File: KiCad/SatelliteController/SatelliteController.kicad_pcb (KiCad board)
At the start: 2 copper layers, 108 parts, among them J1 CONN_ICSP, J10 FROM_CONVERTER, J11 DC_IN, J2 CONN_USB, J3 USB_B_Micro, J4 RJ45, J5 CONN_PRESS, J6 CONN_STATUS_PANEL, J7 CONN_PANEL_BAORD_1, J8 CONN_PANEL_BAORD_2, J9 TO_CONVERTER, Q1 TJ8S06M3L, Q2 2SC3325-Y, Q3 TJ8S06M3L, SW1 SW_RESET, U1 ATMEGA2560-16AUR, U2 FT232RL, U3 LTC485CN8#PBF, U4 U74HC14, U5 NJM7805SDL1, U6 INA219BIDCNT, U7 INA219BIDCNT, Y1 HUSG-16.000-20

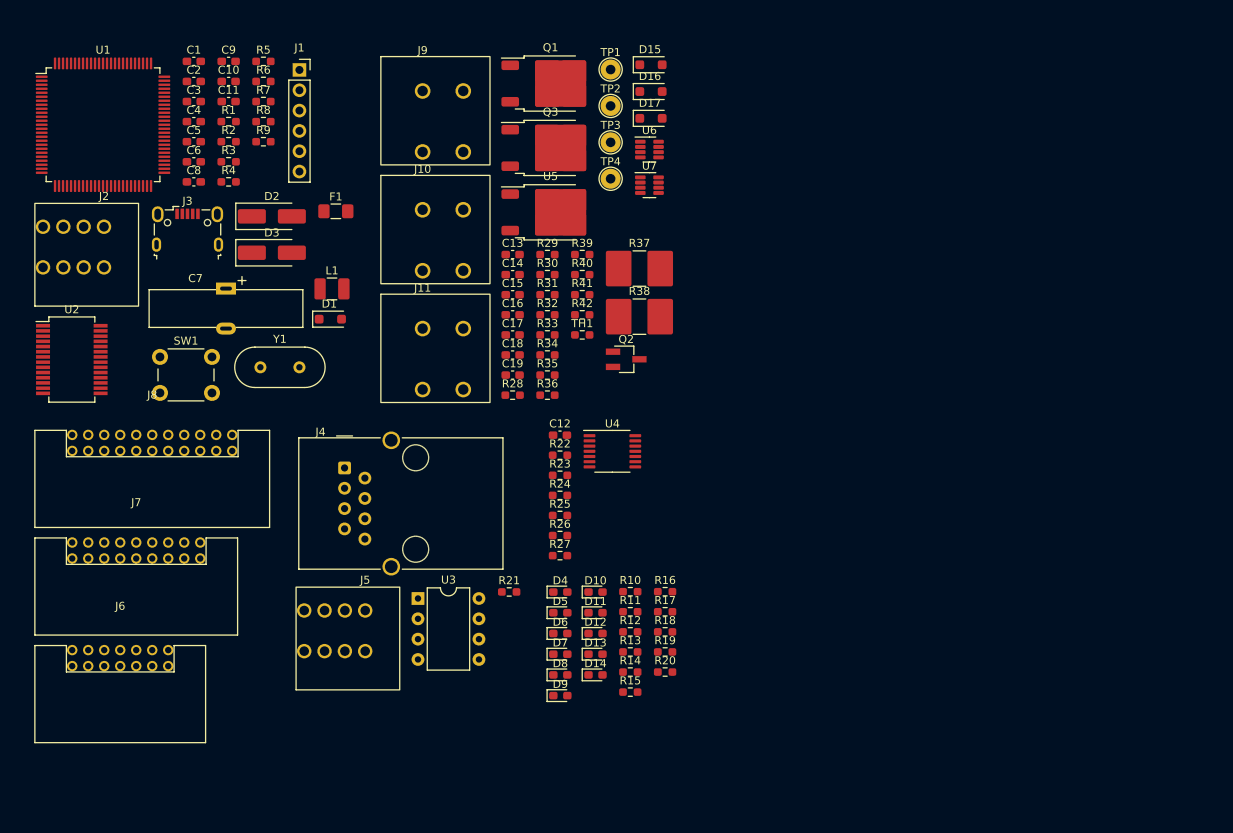
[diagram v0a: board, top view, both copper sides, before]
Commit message: ランコンのKiCadプロジェクトをコピーしてサテコンを作成
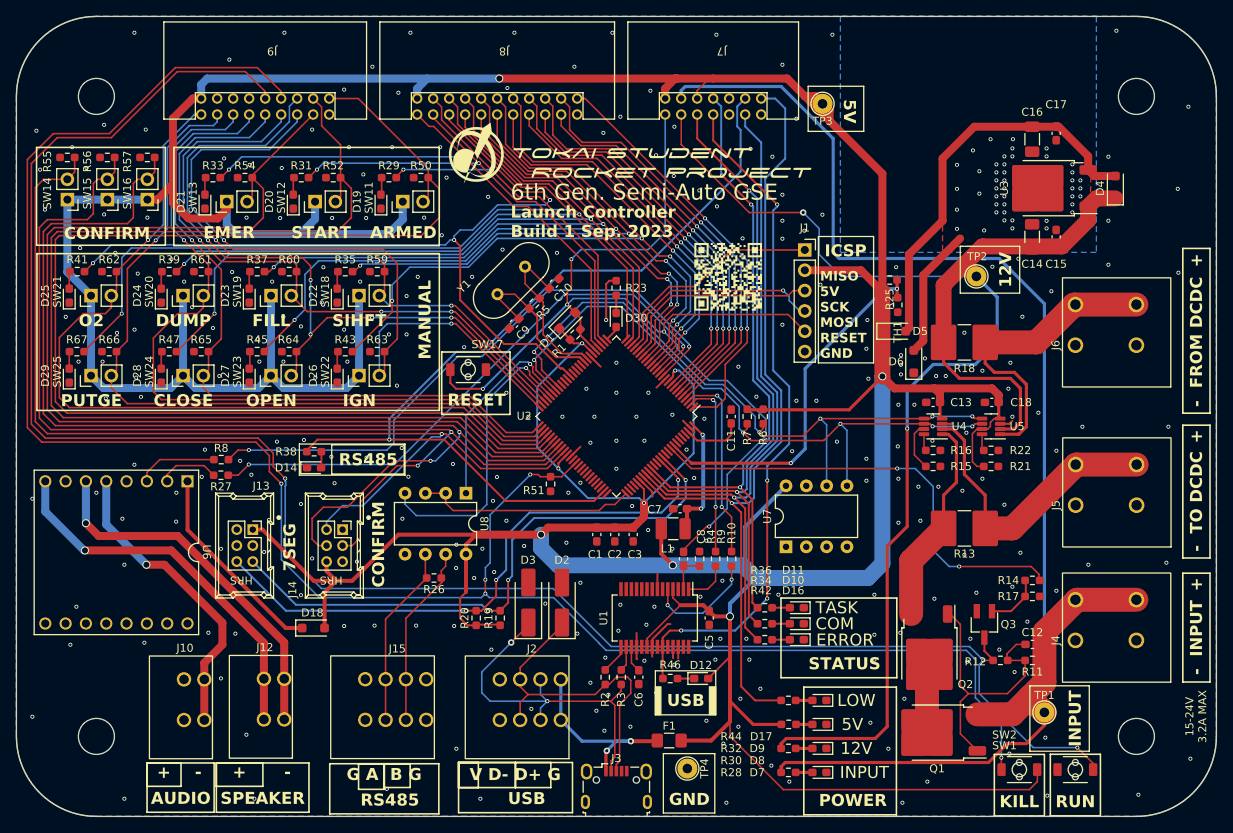
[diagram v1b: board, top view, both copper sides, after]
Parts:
- removed C19, C4: 0.1uF, Capacitor_SMD:C_0603_1608Metric_Pad1.08x0.95mm_HandSolder
- removed D13: LED, LED_SMD:LED_0603_1608Metric_Pad1.05x0.95mm_HandSolder
- removed D15: GS1010FL, Diode_SMD:D_SOD-123F
- removed J11: DC_IN, TSRP_TerminalBlock_Alphaplus:TB411-2-2-E-1
- removed R24: 1kR, Resistor_SMD:R_0603_1608Metric_Pad0.98x0.95mm_HandSolder
- removed R40: 10kR, Resistor_SMD:R_0603_1608Metric_Pad0.98x0.95mm_HandSolder
- added D18: GS1010FL, Diode_SMD:D_SOD-123F, F.Cu at (84.8, 107.3)
- added D19: LED_O, LED_SMD:LED_0603_1608Metric_Pad1.05x0.95mm_HandSolder, F.Cu at (93.2, 54.0)
- added D20: LED_O, LED_SMD:LED_0603_1608Metric_Pad1.05x0.95mm_HandSolder, F.Cu at (82.2, 54.0)
- added D21: LED_O, LED_SMD:LED_0603_1608Metric_Pad1.05x0.95mm_HandSolder, F.Cu at (71.2, 54.0)
- added D22: LED_O, LED_SMD:LED_0603_1608Metric_Pad1.05x0.95mm_HandSolder, F.Cu at (87.7, 65.8)
- added D23: LED_O, LED_SMD:LED_0603_1608Metric_Pad1.05x0.95mm_HandSolder, F.Cu at (76.7, 65.8)
- added D24: LED_O, LED_SMD:LED_0603_1608Metric_Pad1.05x0.95mm_HandSolder, F.Cu at (65.7, 65.8)
- added D25: LED_O, LED_SMD:LED_0603_1608Metric_Pad1.05x0.95mm_HandSolder, F.Cu at (54.2, 65.8)
- added D26: LED_O, LED_SMD:LED_0603_1608Metric_Pad1.05x0.95mm_HandSolder, F.Cu at (87.7, 75.8)
- added D27: LED_O, LED_SMD:LED_0603_1608Metric_Pad1.05x0.95mm_HandSolder, F.Cu at (76.7, 75.8)
- added D28: LED_O, LED_SMD:LED_0603_1608Metric_Pad1.05x0.95mm_HandSolder, F.Cu at (65.7, 75.8)
- added D29: LED_O, LED_SMD:LED_0603_1608Metric_Pad1.05x0.95mm_HandSolder, F.Cu at (54.2, 75.8)
- added D30: LED_O, LED_SMD:LED_0603_1608Metric_Pad1.05x0.95mm_HandSolder, F.Cu at (122.6, 68.8)
- added G***: LOGO, LOGO, F.Cu at (136.6, 63.4)
- added G***: LOGO, LOGO, F.Cu at (124.4, 48.0)
- added J12: CONN_SPEAKER, TSRP_TerminalBlock_Alphaplus:TB401-1-2-E, F.Cu at (78.6, 113.6)
- added J13: CONN_7SEG, TSRP_Connector_Hirose:DF51A-6DP-2DSA, F.Cu at (76.2, 97.0)
- added J14: CONN_BOARD_3, TSRP_Connector_Hirose:DF51A-6DP-2DSA, F.Cu at (87.4, 97.0)
- added J15: CONN_RS485, TSRP_TerminalBlock_Alphaplus:TB401-1-4-E, F.Cu at (95.2, 113.7)
- added R43: 1kR, Resistor_SMD:R_0603_1608Metric_Pad0.98x0.95mm_HandSolder, F.Cu at (88.7, 72.8)
- added R44: 1kR, Resistor_SMD:R_0603_1608Metric_Pad0.98x0.95mm_HandSolder, F.Cu at (144.1, 116.3)
- added R45: 1kR, Resistor_SMD:R_0603_1608Metric_Pad0.98x0.95mm_HandSolder, F.Cu at (77.7, 72.8)
- added R46: 1kR, Resistor_SMD:R_0603_1608Metric_Pad0.98x0.95mm_HandSolder, F.Cu at (129.4, 113.6)
- added R47: 1kR, Resistor_SMD:R_0603_1608Metric_Pad0.98x0.95mm_HandSolder, F.Cu at (66.7, 72.8)
- added R50: 1kR, Resistor_SMD:R_0603_1608Metric_Pad0.98x0.95mm_HandSolder, F.Cu at (98.2, 51.0)
- added R51: 1kR, Resistor_SMD:R_0603_1608Metric_Pad0.98x0.95mm_HandSolder, F.Cu at (114.4, 89.3)
- added R52: 1kR, Resistor_SMD:R_0603_1608Metric_Pad0.98x0.95mm_HandSolder, F.Cu at (87.2, 51.0)
- added R54: 1kR, Resistor_SMD:R_0603_1608Metric_Pad0.98x0.95mm_HandSolder, F.Cu at (76.2, 51.0)
- added R55: 1kR, Resistor_SMD:R_0603_1608Metric_Pad0.98x0.95mm_HandSolder, F.Cu at (54.0, 48.5)
- added R56: 1kR, Resistor_SMD:R_0603_1608Metric_Pad0.98x0.95mm_HandSolder, F.Cu at (59.0, 48.5)
- added R57: 1kR, Resistor_SMD:R_0603_1608Metric_Pad0.98x0.95mm_HandSolder, F.Cu at (64.0, 48.5)
- added R59: 1kR, Resistor_SMD:R_0603_1608Metric_Pad0.98x0.95mm_HandSolder, F.Cu at (92.7, 62.8)
- added R60: 1kR, Resistor_SMD:R_0603_1608Metric_Pad0.98x0.95mm_HandSolder, F.Cu at (81.7, 62.8)
- added R61: 1kR, Resistor_SMD:R_0603_1608Metric_Pad0.98x0.95mm_HandSolder, F.Cu at (70.7, 62.8)
- added R62: 1kR, Resistor_SMD:R_0603_1608Metric_Pad0.98x0.95mm_HandSolder, F.Cu at (59.2, 62.8)
- added R63: 1kR, Resistor_SMD:R_0603_1608Metric_Pad0.98x0.95mm_HandSolder, F.Cu at (92.7, 72.8)
- added R64: 1kR, Resistor_SMD:R_0603_1608Metric_Pad0.98x0.95mm_HandSolder, F.Cu at (81.7, 72.8)
- added R65: 1kR, Resistor_SMD:R_0603_1608Metric_Pad0.98x0.95mm_HandSolder, F.Cu at (70.7, 72.8)
- added R66: 1kR, Resistor_SMD:R_0603_1608Metric_Pad0.98x0.95mm_HandSolder, F.Cu at (59.2, 72.8)
- added R67: 1kR, Resistor_SMD:R_0603_1608Metric_Pad0.98x0.95mm_HandSolder, F.Cu at (55.2, 72.8)
- added REF**: MountingHole_4.5mm, MountingHole:MountingHole_4.5mm, F.Cu at (187.6, 120.8)
- added REF**: MountingHole_4.5mm, MountingHole:MountingHole_4.5mm, F.Cu at (57.6, 40.8)
- added REF**: MountingHole_4.5mm, MountingHole:MountingHole_4.5mm, F.Cu at (57.6, 120.8)
- added REF**: MountingHole_4.5mm, MountingHole:MountingHole_4.5mm, F.Cu at (187.6, 40.8)
- added SW11: SW_Push, Connector_PinHeader_2.54mm:PinHeader_1x02_P2.54mm_Vertical, F.Cu at (95.9, 54.0)
- added SW12: SW_Push, Connector_PinHeader_2.54mm:PinHeader_1x02_P2.54mm_Vertical, F.Cu at (85.0, 54.0)
- added SW13: SW_Push, Connector_PinHeader_2.54mm:PinHeader_1x02_P2.54mm_Vertical, F.Cu at (73.9, 54.0)
- added SW14: SW_Push, Connector_PinHeader_2.54mm:PinHeader_1x02_P2.54mm_Vertical, F.Cu at (54.0, 53.8)
- added SW15: SW_Push, Connector_PinHeader_2.54mm:PinHeader_1x02_P2.54mm_Vertical, F.Cu at (59.0, 53.8)
- added SW16: SW_Push, Connector_PinHeader_2.54mm:PinHeader_1x02_P2.54mm_Vertical, F.Cu at (64.0, 53.8)
- added SW17: SW_Push, TSRP_Button_Switch_SMD:TVAF06-A020B-R, F.Cu at (104.1, 75.0)
- added SW18: SW_Push, Connector_PinHeader_2.54mm:PinHeader_1x02_P2.54mm_Vertical, F.Cu at (90.5, 65.8)
- added SW19: SW_Push, Connector_PinHeader_2.54mm:PinHeader_1x02_P2.54mm_Vertical, F.Cu at (79.5, 65.8)
- added SW2: SW_Push, TSRP_Button_Switch_SMD:TVAF06-A020B-R, F.Cu at (173.0, 125.0)
- added SW20: SW_Push, Connector_PinHeader_2.54mm:PinHeader_1x02_P2.54mm_Vertical, F.Cu at (68.5, 65.8)
- added SW21: SW_Push, Connector_PinHeader_2.54mm:PinHeader_1x02_P2.54mm_Vertical, F.Cu at (57.0, 65.8)
- added SW22: SW_Push, Connector_PinHeader_2.54mm:PinHeader_1x02_P2.54mm_Vertical, F.Cu at (90.5, 75.8)
- added SW23: SW_Push, Connector_PinHeader_2.54mm:PinHeader_1x02_P2.54mm_Vertical, F.Cu at (79.5, 75.8)
- added SW24: SW_Push, Connector_PinHeader_2.54mm:PinHeader_1x02_P2.54mm_Vertical, F.Cu at (68.5, 75.8)
- added SW25: SW_Push, Connector_PinHeader_2.54mm:PinHeader_1x02_P2.54mm_Vertical, F.Cu at (57.0, 75.8)
- added U8: LTC485CN8#PBF, Package_DIP:DIP-8_W7.62mm, F.Cu at (103.8, 90.4)
- C1, C2: value 15pF -> 0.1uF
- C10, C9: value 0.1uF -> 15pF
- C14, C16: footprint Capacitor_SMD:C_0603_1608Metric_Pad1.08x0.95mm_HandSolder -> Capacitor_SMD:C_1206_3216Metric_Pad1.33x1.80mm_HandSolder
- C7: value 1F -> 0.1uF; footprint Capacitor_THT:DX_5R5VxxxxU_D19.0mm_P5.00mm -> Capacitor_SMD:C_0603_1608Metric_Pad1.08x0.95mm_HandSolder
- D10, D11: value LED -> LED_G
- D12, D14: value LED -> LED_B
- D16, D17: value SS2040FL -> LED_R; footprint Diode_SMD:D_SOD-123F -> LED_SMD:LED_0603_1608Metric_Pad1.05x0.95mm_HandSolder
- D4: value LED -> GS1010FL; footprint LED_SMD:LED_0603_1608Metric_Pad1.05x0.95mm_HandSolder -> Diode_SMD:D_SOD-123F
- D5, D6: value LED -> SS2040FL; footprint LED_SMD:LED_0603_1608Metric_Pad1.05x0.95mm_HandSolder -> Diode_SMD:D_SOD-123F
- D7, D8, D9: value LED -> LED_O
- J10: value FROM_CONVERTER -> CONN_AUDIO; footprint TSRP_TerminalBlock_Alphaplus:TB411-2-2-E-1 -> TSRP_TerminalBlock_Alphaplus:TB401-1-2-E
- J4: value RJ45 -> DC_IN; footprint Connector_RJ:RJ45_Wuerth_7499010001A_Horizontal -> TSRP_TerminalBlock_Alphaplus:TB411-2-2-E-1
- J5: value CONN_PRESS -> TO_CONVERTER; footprint TSRP_TerminalBlock_Alphaplus:TB401-1-4-E -> TSRP_TerminalBlock_Alphaplus:TB411-2-2-E-1
- J6: value CONN_STATUS_PANEL -> FROM_CONVERTER; footprint TSRP_Connector_Hirose:DF51A-14DP-2DS -> TSRP_TerminalBlock_Alphaplus:TB411-2-2-E-1
- J7: value CONN_PANEL_BAORD_1 -> CONN_STATUS_PANEL; footprint TSRP_Connector_Hirose:DF51A-18DP-2DS -> TSRP_Connector_Hirose:DF51A-14DP-2DS
- J9: value TO_CONVERTER -> CONN_PANEL_BAORD_1; footprint TSRP_TerminalBlock_Alphaplus:TB411-2-2-E-1 -> TSRP_Connector_Hirose:DF51A-18DP-2DS
- Q2: value 2SC3325-Y -> TJ8S06M3L; footprint Package_TO_SOT_SMD:SC-59_Handsoldering -> Package_TO_SOT_SMD:TO-252-2
- Q3: value TJ8S06M3L -> 2SC3325-Y; footprint Package_TO_SOT_SMD:TO-252-2 -> Package_TO_SOT_SMD:SC-59_Handsoldering
- R10: value 3.6kR -> 1kR
- R11: value 1kR -> 5.6R
- R12: value 2.4kR -> 3.3R
- R13, R18: value 1kR -> 0.1R2W; footprint Resistor_SMD:R_0603_1608Metric_Pad0.98x0.95mm_HandSolder -> Resistor_SMD:R_2816_7142Metric_Pad3.20x4.45mm_HandSolder
- R14, R15, R16, R17, R19, R20, R22, R25: value 1kR -> 10kR
- R2: value 1MR -> 22R
- R21: value 120R -> 10kR
- R26: value 1kR -> 120R
- R28: value 5.6R -> 3.6kR
- R29: value 3.3R -> 1kR
- R3: value 1kR -> 22R
- R30: value 10kR -> 2.4kR
- R31: value 2.2kR -> 1kR
- R32: value 12kR -> 1kR
- R33, R35: value 2kR -> 1kR
- R34: value 12kR -> 2.2kR
- R36: value 10kR -> 2.2kR
- R37, R38: value 0.1R2W -> 1kR; footprint Resistor_SMD:R_2816_7142Metric_Pad3.20x4.45mm_HandSolder -> Resistor_SMD:R_0603_1608Metric_Pad0.98x0.95mm_HandSolder
- R39, R41, R42: value 10kR -> 1kR
- R5: value 10kR -> 1MR
- R7: value 22R -> 10kR
- R8: value 22R -> 1kR
- SW1: value SW_RESET -> SW_Push; footprint Button_Switch_THT:SW_PUSH_6mm_H7.3mm -> TSRP_Button_Switch_SMD:TVAF06-A020B-R
- U1: value ATMEGA2560-16AUR -> FT232RL; footprint Package_QFP:TQFP-100_14x14mm_P0.5mm -> Package_SO:SSOP-28_5.3x10.2mm_P0.65mm
- U2: value FT232RL -> ATMEGA2560-16AUR; footprint Package_SO:SSOP-28_5.3x10.2mm_P0.65mm -> Package_QFP:TQFP-100_14x14mm_P0.5mm
- U3: value LTC485CN8#PBF -> NJM7805SDL1; footprint Package_DIP:DIP-8_W7.62mm -> Package_TO_SOT_SMD:TO-252-2
- U4: value U74HC14 -> INA219BIDCNT; footprint Package_SO:TSSOP-14_4.4x5mm_P0.65mm -> Package_TO_SOT_SMD:SOT-23-8
- U5: value NJM7805SDL1 -> INA219BIDCNT; footprint Package_TO_SOT_SMD:TO-252-2 -> Package_TO_SOT_SMD:SOT-23-8
- U6: value INA219BIDCNT -> DFPlayer; footprint Package_TO_SOT_SMD:SOT-23-8 -> TSRP_Module:DFPlayer-mini
- U7: value INA219BIDCNT -> 24LC256; footprint Package_TO_SOT_SMD:SOT-23-8 -> Package_DIP:DIP-8_W7.62mm
- moved J6 133.6 mm to (182.6, 71.9), turned to 90 degrees
- moved SW1 125.5 mm to (180.0, 125.0)
- moved J7 101.4 mm to (140.7, 43.1), turned to 180 degrees
- moved TP1 96.9 mm to (176.1, 117.8)
- moved J4 96.4 mm to (182.6, 108.8), turned to 90 degrees
- moved Q1 94.4 mm to (162.7, 120.4), turned to 180 degrees
- moved U3 94.0 mm to (176.6, 52.3), turned to 180 degrees
- moved U1 92.5 mm to (127.4, 106.0), turned to -90 degrees
- moved J5 92.4 mm to (182.7, 91.9), turned to 90 degrees
- moved J3 87.9 mm to (122.6, 127.1)
- moved C5 87.7 mm to (134.2, 106.0), turned to 90 degrees
- moved D4 85.9 mm to (185.0, 52.2), turned to 90 degrees
- moved C6 85.1 mm to (125.4, 113.4), turned to 90 degrees
- moved R2 81.8 mm to (121.2, 113.4), turned to 90 degrees
- moved R3 81.0 mm to (123.2, 113.4), turned to -90 degrees
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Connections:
- C1 pad 1: GND -> CONN_LED_5V
- C1 pad 2: Net-(U1-XTAL1) -> GND
- C10 pad 2: +5V -> Net-(U2-XTAL2)
- C11 pad 1: Net-(U2-DTR) -> GND
- C11 pad 2: CTL_RESET -> Net-(U2-AREF)
- C12 pad 1: GND -> CONN_LED_INPUT
- C12 pad 2: +5V -> Net-(Q1-G)
- C13 pad 1: CONN_LED_INPUT -> CONN_LED_5V
- C13 pad 2: Net-(Q1-G) -> GND
- C14 pad 1: Net-(D16-A) -> Net-(D6-A)
- C15 pad 1: Net-(D16-A) -> Net-(D6-A)
- C16 pad 1: Net-(D16-A) -> Net-(D6-A)
- C16 pad 2: Net-(D15-A) -> Net-(D4-A)
- C17 pad 1: Net-(D16-A) -> Net-(D6-A)
- C17 pad 2: Net-(D15-A) -> Net-(D4-A)
- C2 pad 1: GND -> CONN_LED_5V
- C2 pad 2: Net-(U1-XTAL2) -> GND
- C3 pad 1: GND -> CONN_LED_5V
- C3 pad 2: Net-(U1-AREF) -> GND
- C5 pad 1: +5V -> GND
- C5 pad 2: GND -> CONN_LED_5V
- C6 pad 1: +5V -> GND
- C6 pad 2: GND -> Net-(U1-3V3OUT)
- C7 pad 1: +5V -> Net-(U2-AVCC)
- C8 pad 1: Net-(U1-AVCC) -> Net-(U1-DTR)
- C8 pad 2: GND -> CTL_RESET
- C9 pad 2: Net-(U2-3V3OUT) -> Net-(U2-XTAL1)
- D1 pad 1: +5V -> CONN_LED_5V
- D12 pad 1: GND -> Net-(D12-K)
- D12 pad 2: Net-(D12-A) -> CONN_LED_5V
- D17 pad 1: CONN_LED_5V -> GND
- D17 pad 2: Net-(D15-A) -> Net-(D17-A)
- D2 pad 1: GND -> USB_D+
- D2 pad 2: USB_D+ -> GND
- D3 pad 1: GND -> USB_D-
- D3 pad 2: USB_D- -> GND
- D4 pad 1: GND -> CONN_LED_12V
- D5 pad 1: Net-(D5-K) -> CONN_LED_5V
- D5 pad 2: +5V -> Net-(D4-A)
- D7 pad 1: Net-(D7-K) -> GND
- D7 pad 2: +5V -> Net-(D7-A)
- F1 pad 2: +5V -> CONN_LED_5V
- J1 pad 2: +5V -> CONN_LED_5V
- J10 pad 2: FROM_CONVERTER -> Net-(J10-Pin_2)
- J4 pad 2: GND -> CONN_LED_INPUT
- J5 pad 1: +12V -> GND
- J5 pad 2: unconnected-(J5-Pin_2-Pad2) -> TO_CONVERTER
- J6 pad 2: CONN_LED_LOW_VOLTAGE -> FROM_CONVERTER
- J7 pad 10: unconnected-(J7-Pin_10-Pad10) -> CONN_LED_5V
- J7 pad 11: unconnected-(J7-Pin_11-Pad11) -> CONN_LED_12V
- J7 pad 12: unconnected-(J7-Pin_12-Pad12) -> CONN_LED_INPUT
- J7 pad 13: unconnected-(J7-Pin_13-Pad13) -> CTL_RESET
- J7 pad 14: unconnected-(J7-Pin_14-Pad14) -> CONN_LED_5V
- J7 pad 2: unconnected-(J7-Pin_2-Pad2) -> CONN_LED_LOW_VOLTAGE
- J7 pad 3: unconnected-(J7-Pin_3-Pad3) -> CONN_LED_ERROR
- J7 pad 4: unconnected-(J7-Pin_4-Pad4) -> CONN_LED_RS485_ACCESS
- J7 pad 7: unconnected-(J7-Pin_7-Pad7) -> CONN_LED_USB_ACCESS
- J7 pad 8: unconnected-(J7-Pin_8-Pad8) -> CONN_LED_TASK
- J7 pad 9: unconnected-(J7-Pin_9-Pad9) -> CONN_LED_COM
- J8 pad 10: unconnected-(J8-Pin_10-Pad10) -> CONN_LED_FB_PURGE
- J8 pad 11: unconnected-(J8-Pin_11-Pad11) -> CONN_LED_SHIFT
- J8 pad 12: unconnected-(J8-Pin_12-Pad12) -> CONN_LED_IGNITOR
- J8 pad 13: unconnected-(J8-Pin_13-Pad13) -> CONN_LED_FILL
- J8 pad 14: unconnected-(J8-Pin_14-Pad14) -> CONN_LED_OPEN
- J8 pad 15: unconnected-(J8-Pin_15-Pad15) -> CONN_LED_DUMP
- J8 pad 16: unconnected-(J8-Pin_16-Pad16) -> CONN_LED_CLOSE
- J8 pad 17: unconnected-(J8-Pin_17-Pad17) -> CONN_LED_O2
- J8 pad 18: unconnected-(J8-Pin_18-Pad18) -> CONN_LED_PURGE
- J8 pad 19: unconnected-(J8-Pin_19-Pad19) -> CONN_LED_SEQUENCE
- J8 pad 2: unconnected-(J8-Pin_2-Pad2) -> CONN_LED_POWER
- J8 pad 20: unconnected-(J8-Pin_20-Pad20) -> CONN_LED_SAFTEY
- J8 pad 21: unconnected-(J8-Pin_21-Pad21) -> CONN_LED_EMERGENCY
- J8 pad 22: +5V -> CONN_LED_5V
- J8 pad 3: unconnected-(J8-Pin_3-Pad3) -> CONN_LED_FB_SHIFT
- J8 pad 4: unconnected-(J8-Pin_4-Pad4) -> CONN_LED_FB_IGNITOR
- J8 pad 5: unconnected-(J8-Pin_5-Pad5) -> CONN_LED_FB_FILL
- J8 pad 6: unconnected-(J8-Pin_6-Pad6) -> CONN_LED_FB_OPEN
- J8 pad 7: unconnected-(J8-Pin_7-Pad7) -> CONN_LED_FB_DUMP
- J8 pad 8: unconnected-(J8-Pin_8-Pad8) -> CONN_LED_FB_CLOSE
- J8 pad 9: unconnected-(J8-Pin_9-Pad9) -> CONN_LED_FB_O2
- J9 pad 2: TO_CONVERTER -> CTL_SAFETY
- L1 pad 1: Net-(U1-AVCC) -> Net-(U2-AVCC)
- L1 pad 2: +5V -> CONN_LED_5V
- Q2 pad 1: Net-(Q2-B) -> Net-(Q1-G)
- Q2 pad 2: GND -> Net-(Q1-D)
- Q2 pad 3: CTL_RUN -> +VSW
- Q3 pad 1: Net-(Q1-G) -> Net-(Q3-B)
- Q3 pad 2: Net-(Q1-D) -> GND
- Q3 pad 3: +VSW -> CTL_RUN
- R1 pad 1: +5V -> CONN_LED_5V
- R10 pad 1: CONN_LED_INPUT -> UART0_TX
- R10 pad 2: Net-(D4-A) -> Net-(U2-PE1)
- R11 pad 1: Net-(D5-K) -> CONN_LED_INPUT
- R11 pad 2: CONN_LED_USB_TX -> Net-(Q1-G)
- R12 pad 1: CONN_LED_12V -> Net-(Q1-G)
- R12 pad 2: Net-(D6-A) -> CTL_RUN
- R13 pad 1: Net-(D7-K) -> TO_CONVERTER
- R13 pad 2: CONN_LED_USB_RX -> +VSW
- R14 pad 1: CONN_LED_5V -> CTL_POWER
- R14 pad 2: Net-(D8-A) -> Net-(Q3-B)
- R15 pad 1: CONN_LED_RS485_TX -> Net-(U4-A0)
- R15 pad 2: Net-(D9-A) -> GND
- R16 pad 1: CONN_LED_COM -> GND
- R16 pad 2: Net-(D10-A) -> Net-(U4-A1)
- R17 pad 1: CONN_LED_RS485_RX -> Net-(Q3-B)
- R17 pad 2: Net-(D11-A) -> GND
- R18 pad 1: CONN_LED_TASK -> CONN_LED_12V
- R18 pad 2: Net-(D12-A) -> FROM_CONVERTER
- R19 pad 1: CONN_LED_CAUTION -> CONN_LED_5V
- R19 pad 2: Net-(D13-A) -> 7SEG_CLK
- R2 pad 1: Net-(U1-XTAL1) -> USB_D+
- R2 pad 2: Net-(U1-XTAL2) -> Net-(U1-USBD+)
- R20 pad 1: CONN_LED_LOW_VOLTAGE -> CONN_LED_5V
- R20 pad 2: Net-(D14-A) -> 7SEG_DIO
- R21 pad 1: Net-(U3-B) -> CONN_LED_5V
- R21 pad 2: Net-(U3-A) -> GND
- R22 pad 1: SW_RUN -> GND
- R22 pad 2: Net-(R22-Pad2) -> Net-(U5-A1)
- R23 pad 1: SW_KILL -> Net-(D30-K)
- R23 pad 2: Net-(R23-Pad2) -> GND
- R25 pad 1: SW_RESET -> VREF_THERMISTOR
- R25 pad 2: Net-(R25-Pad2) -> CONN_LED_5V
- R26 pad 1: SW_PURGE -> Net-(J15-Pin_3)
- R26 pad 2: Net-(R26-Pad2) -> Net-(J15-Pin_2)
- R27 pad 1: GND -> Net-(U2-PH1)
- R27 pad 2: Net-(R27-Pad2) -> UART2_TX
- R28 pad 2: Net-(Q1-G) -> Net-(D7-A)
- R29 pad 1: Net-(Q1-G) -> CONN_LED_SAFTEY
- R29 pad 2: CTL_RUN -> Net-(D19-A)
- R3 pad 1: Net-(U1-PE0) -> Net-(U1-USBD-)
- R3 pad 2: UART0_RX -> USB_D-
- R30 pad 1: Net-(Q2-B) -> CONN_LED_12V
- R30 pad 2: GND -> Net-(D8-A)
- R31 pad 1: CTL_POWER -> CONN_LED_SEQUENCE
- R31 pad 2: Net-(Q2-B) -> Net-(D20-A)
- R32 pad 1: VREF_VSW -> CONN_LED_5V
- R32 pad 2: +VSW -> Net-(D9-A)
- R33 pad 1: GND -> CONN_LED_EMERGENCY
- R33 pad 2: VREF_VSW -> Net-(D21-A)
- R34 pad 1: VREF_12V -> CONN_LED_COM
- R34 pad 2: CONN_LED_12V -> Net-(D10-A)
- R35 pad 1: GND -> CONN_LED_SHIFT
- R35 pad 2: VREF_12V -> Net-(D22-A)
- R36 pad 1: GND -> CONN_LED_TASK
- R36 pad 2: VREF_THERMISTOR -> Net-(D11-A)
- R37 pad 1: TO_CONVERTER -> CONN_LED_FILL
- R37 pad 2: +VSW -> Net-(D23-A)
- R38 pad 1: CONN_LED_12V -> CONN_LED_RS485_ACCESS
- R38 pad 2: FROM_CONVERTER -> Net-(D14-A)
- R39 pad 1: Net-(U6-A0) -> CONN_LED_DUMP
- R39 pad 2: GND -> Net-(D24-A)
- R4 pad 1: UART0_TX -> Net-(U1-DTR)
- R4 pad 2: Net-(U1-PE1) -> GND
- R41 pad 1: CONN_LED_5V -> CONN_LED_O2
- R41 pad 2: GND -> Net-(D25-A)
- R42 pad 1: GND -> CONN_LED_ERROR
- R42 pad 2: Net-(U7-A1) -> Net-(D16-A)
- R5 pad 1: +5V -> Net-(U2-XTAL1)
- R5 pad 2: I2C_SCL -> Net-(U2-XTAL2)
- R6 pad 1: +5V -> CONN_LED_5V
- R6 pad 2: I2C_SDA -> I2C_SCL
- R7 pad 1: USB_D+ -> CONN_LED_5V
- R7 pad 2: Net-(U2-USBD+) -> I2C_SDA
- R8 pad 1: Net-(U2-USBD-) -> UART2_RX
- R8 pad 2: USB_D- -> Net-(U2-PH0)
- R9 pad 1: Net-(U2-DTR) -> Net-(U2-PE0)
- R9 pad 2: GND -> UART0_RX
- SW1 pad 2: CTL_RESET -> CTL_RUN
- TH1 pad 1: CONN_LED_5V -> VREF_THERMISTOR
- TH1 pad 2: VREF_THERMISTOR -> GND
- U1 pad 1: unconnected-(U1-PG5-Pad1) -> UART0_RX
- U1 pad 10: +5V -> unconnected-(U1-DCD-Pad10)
- U1 pad 11: GND -> unconnected-(U1-CTS-Pad11)
- U1 pad 15: unconnected-(U1-PH3-Pad15) -> Net-(U1-USBD+)
- U1 pad 16: unconnected-(U1-PH4-Pad16) -> Net-(U1-USBD-)
- U1 pad 17: unconnected-(U1-PH5-Pad17) -> Net-(U1-3V3OUT)
- U1 pad 18: unconnected-(U1-PH6-Pad18) -> GND
- U1 pad 2: Net-(U1-PE0) -> Net-(U1-DTR)
- U1 pad 20: SPI_SCK -> CONN_LED_5V
- U1 pad 21: SPI_MOSI -> GND
- U1 pad 22: SPI_MISO -> CONN_LED_USB_ACCESS
- U1 pad 23: unconnected-(U1-PB4-Pad23) -> CONN_LED_USB_ACCESS
- U1 pad 24: unconnected-(U1-PB5-Pad24) -> (no net)
- U1 pad 25: unconnected-(U1-PB6-Pad25) -> GND
- U1 pad 26: unconnected-(U1-PB7-Pad26) -> GND
- U1 pad 3: Net-(U1-PE1) -> unconnected-(U1-RTS-Pad3)
- U1 pad 4: unconnected-(U1-PE2-Pad4) -> CONN_LED_5V
- U1 pad 5: unconnected-(U1-PE3-Pad5) -> UART0_TX
- U1 pad 7: unconnected-(U1-PE5-Pad7) -> GND
- U1 pad 8: unconnected-(U1-PE6-Pad8) -> (no net)
- U2 pad 1: UART0_RX -> CONN_LED_POWER
- U2 pad 10: unconnected-(U2-DCD-Pad10) -> CONN_LED_5V
- U2 pad 11: unconnected-(U2-CTS-Pad11) -> GND
- U2 pad 12: unconnected-(U2-CBUS4-Pad12) -> Net-(U2-PH0)
- U2 pad 13: unconnected-(U2-CBUS2-Pad13) -> Net-(U2-PH1)
- U2 pad 14: unconnected-(U2-CBUS3-Pad14) -> CONN_LED_FB_PURGE
- U2 pad 15: Net-(U2-USBD+) -> CONN_LED_FB_O2
- U2 pad 16: Net-(U2-USBD-) -> CONN_LED_IGNITOR
- U2 pad 17: Net-(U2-3V3OUT) -> CONN_LED_SHIFT
- U2 pad 18: GND -> CONN_LED_OPEN
- U2 pad 19: unconnected-(U2-~{RESET}-Pad19) -> CONN_LED_FILL
- U2 pad 2: Net-(U2-DTR) -> Net-(U2-PE0)
- U2 pad 20: +5V -> SPI_SCK
- U2 pad 21: GND -> SPI_MOSI
- U2 pad 22: CONN_LED_USB_RX -> SPI_MISO
- U2 pad 23: CONN_LED_USB_TX -> CONN_LED_CLOSE
- U2 pad 24: (no net) -> CONN_LED_DUMP
- U2 pad 25: GND -> CONN_LED_PURGE
- U2 pad 26: GND -> Net-(D30-A)
- U2 pad 27: unconnected-(U2-OSCI-Pad27) -> CONN_LED_SAFTEY
- U2 pad 28: unconnected-(U2-OSCO-Pad28) -> CONN_LED_SEQUENCE
- U2 pad 3: unconnected-(U2-RTS-Pad3) -> Net-(U2-PE1)
- U2 pad 4: +5V -> CONN_LED_FB_IGNITOR
- U2 pad 5: UART0_TX -> CONN_LED_FB_SHIFT
- U2 pad 6: unconnected-(U2-RI-Pad6) -> CONN_LED_FB_OPEN
- U2 pad 7: GND -> CONN_LED_FB_FILL
- U2 pad 8: (no net) -> CONN_LED_FB_CLOSE
- U2 pad 9: unconnected-(U2-DCR-Pad9) -> CONN_LED_FB_DUMP
- U3 pad 1: UART1_RX -> CONN_LED_12V
- U3 pad 2: CTL_RS485_DERE -> Net-(D6-A)
- U3 pad 3: CTL_RS485_DERE -> Net-(D4-A)
- U4 pad 1: Net-(R22-Pad2) -> +VSW
- U4 pad 2: CTL_RUN -> TO_CONVERTER
- U4 pad 3: Net-(R23-Pad2) -> GND
- U4 pad 4: CTL_KILL -> CONN_LED_5V
- U4 pad 5: Net-(R24-Pad2) -> I2C_SCL
- U4 pad 6: CTL_SAFETY -> I2C_SDA
- U4 pad 7: GND -> Net-(U4-A0)
- U4 pad 8: CTL_RESET -> Net-(U4-A1)
- U5 pad 1: CONN_LED_12V -> FROM_CONVERTER
- U5 pad 2: Net-(D16-A) -> CONN_LED_12V
- U5 pad 3: Net-(D15-A) -> GND
- U6 pad 1: +VSW -> Net-(D18-K)
- U6 pad 2: TO_CONVERTER -> UART2_TX
- U6 pad 3: GND -> UART2_RX
- U6 pad 4: CONN_LED_5V -> unconnected-(U6-DAC_R-Pad4)
- U6 pad 5: I2C_SCL -> Net-(J10-Pin_2)
- U6 pad 6: I2C_SDA -> Net-(J12-Pin_2)
- U6 pad 7: Net-(U6-A0) -> GND
- U7 pad 1: FROM_CONVERTER -> GND
- U7 pad 2: CONN_LED_12V -> GND
- U7 pad 4: CONN_LED_5V -> GND
- U7 pad 5: I2C_SCL -> I2C_SDA
- U7 pad 6: I2C_SDA -> I2C_SCL
- U7 pad 7: CONN_LED_5V -> GND
- U7 pad 8: Net-(U7-A1) -> CONN_LED_5V
- Y1 pad 1: Net-(U1-XTAL2) -> Net-(U2-XTAL2)
- Y1 pad 2: Net-(U1-XTAL1) -> Net-(U2-XTAL1)
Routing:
- net CONN_LED_5V: track 0.00 -> 691.7 mm, vias 0 -> 9
- net CTL_KILL: track 0.00 -> 248.6 mm, vias 0 -> 5
- net CTL_RUN: track 0.00 -> 233.7 mm, vias 0 -> 3
- net CONN_LED_12V: track 0.00 -> 187.1 mm, vias 0 -> 2
- net CONN_LED_INPUT: track 0.00 -> 186.9 mm
- net CTL_SAFETY: track 0.00 -> 160.3 mm
- net CTL_SEQUENCE_START: track 0.00 -> 145.1 mm
- net CTL_CONFIRM_3: track 0.00 -> 139.7 mm, vias 0 -> 2
- net CTL_EMERGENCY_STOP: track 0.00 -> 136.1 mm
- net CTL_RESET: track 0.00 -> 134.3 mm, vias 0 -> 5
- net CTL_CONFIRM_2: track 0.00 -> 130.7 mm, vias 0 -> 2
- net CTL_CONFIRM_1: track 0.00 -> 126.3 mm, vias 0 -> 1
- net CONN_LED_PURGE: track 0.00 -> 113.0 mm, vias 0 -> 2
- net CONN_LED_RS485_ACCESS: track 0.00 -> 110.5 mm, vias 0 -> 1
- net CTL_O2: track 0.00 -> 108.8 mm, vias 0 -> 1
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- added copper zone on B.Cu, net GND
- added copper zone on F.Cu, net GND
- added copper zone on B.Cu, net Net-(D6-A)
- added copper zone on F.Cu, net Net-(D6-A)
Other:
- board outline added: 150 x 100 mm
- board text added: "+"
- board text added: "-"
- board text added: "12V"
- board text added: "15-24V 3.2A MAX"
- board text added: "5V"
- board text added: "6th Gen. Semi-Auto GSE"
- board text added: "7SEG"
- board text added: "ARMED"
- board text added: "AUDIO"
- board text added: "CLOSE"
- board text added: "COM"
- board text added: "CONFIRM"
- board text added: "DUMP"
- board text added: "EMER"
- board text added: "ERROR"
- board text added: "FILL"
- board text added: "FROM DCDC"
- board text added: "G A B G"
- board text added: "GND"
- board text added: "ICSP"
- board text added: "IGN"
- board text added: "INPUT"
- board text added: "J4"
- board text added: "J5"
- board text added: "KILL"
- board text added: "LOW"
- board text added: "Launch Controller Build 1 Sep. 2023"
- board text added: "MANUAL"
- board text added: "MISO 5V SCK MOSI RESET GND"
- board text added: "O2"
- board text added: "OPEN"
- board text added: "POWER"
- board text added: "PUTGE"
- board text added: "RESET"
- board text added: "RS485"
- board text added: "RUN"
- board text added: "SIHFT"
- board text added: "SPEAKER"
- board text added: "START"
- board text added: "STATUS"
- board text added: "TASK"
- board text added: "TO DCDC"
- board text added: "USB"
- board text added: "V D- D+ G"

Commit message: 音声完成を削除
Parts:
- removed D18: GS1010FL, Diode_SMD:D_SOD-123F
- removed J10: CONN_AUDIO, TSRP_TerminalBlock_Alphaplus:TB401-1-2-E
- removed J12: CONN_SPEAKER, TSRP_TerminalBlock_Alphaplus:TB401-1-2-E
- removed R27, R8: 1kR, Resistor_SMD:R_0603_1608Metric_Pad0.98x0.95mm_HandSolder
- removed U6: DFPlayer, TSRP_Module:DFPlayer-mini
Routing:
- net Net-(U2-PH0): track 76.2 -> 0.00 mm, vias 2 -> 0
- net Net-(U2-PH1): track 73.6 -> 0.00 mm, vias 2 -> 0
- net Net-(J12-Pin_1): track 47.5 -> 0.00 mm, vias 1 -> 0
- net Net-(J12-Pin_2): track 45.8 -> 0.00 mm, vias 1 -> 0
- net Net-(J10-Pin_2): track 38.1 -> 0.00 mm, vias 1 -> 0
- net Net-(D18-K): track 25.5 -> 0.00 mm
- net UART2_RX: track 10.1 -> 0.00 mm
- net UART2_TX: track 7.60 -> 0.00 mm
- net CONN_LED_5V: track 691.7 -> 685.2 mm
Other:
- board text removed: "AUDIO"
- board text removed: "SPEAKER"

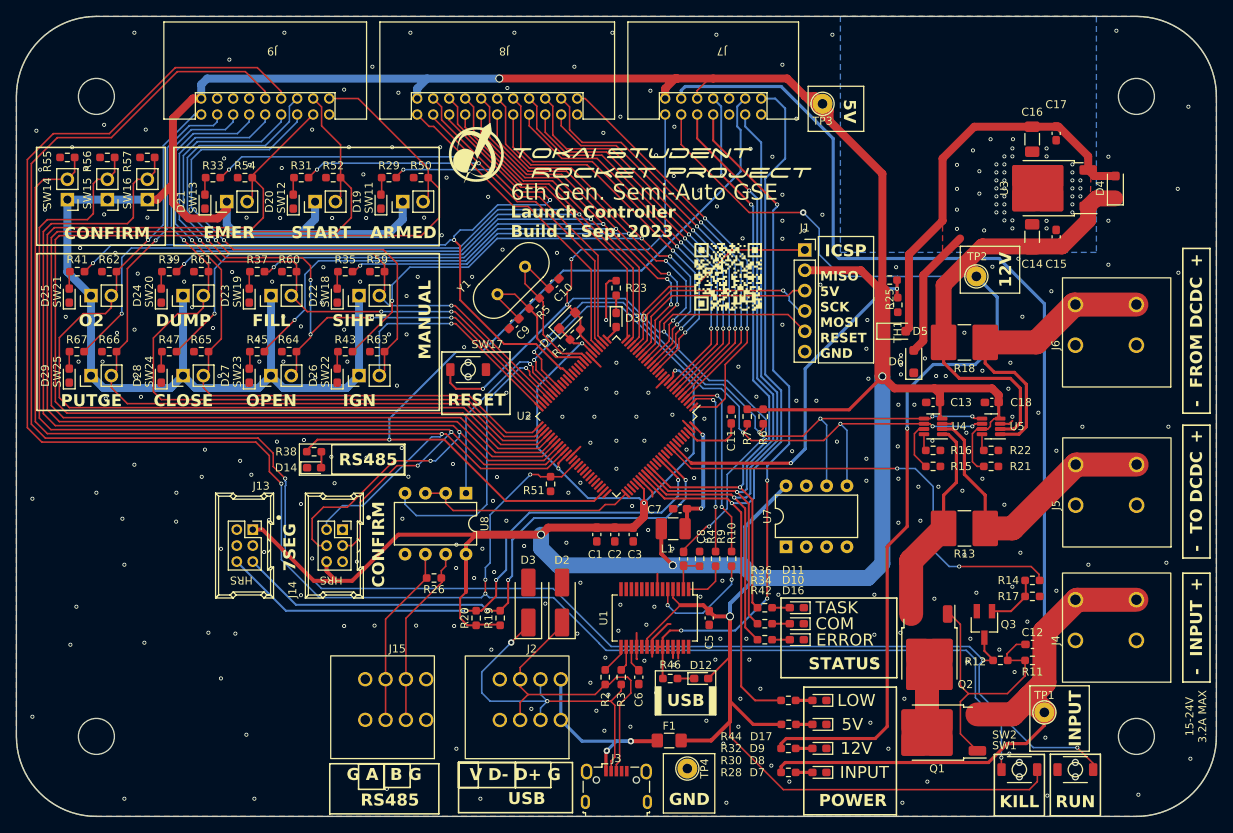
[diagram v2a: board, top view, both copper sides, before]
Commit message: 手動操作を削除
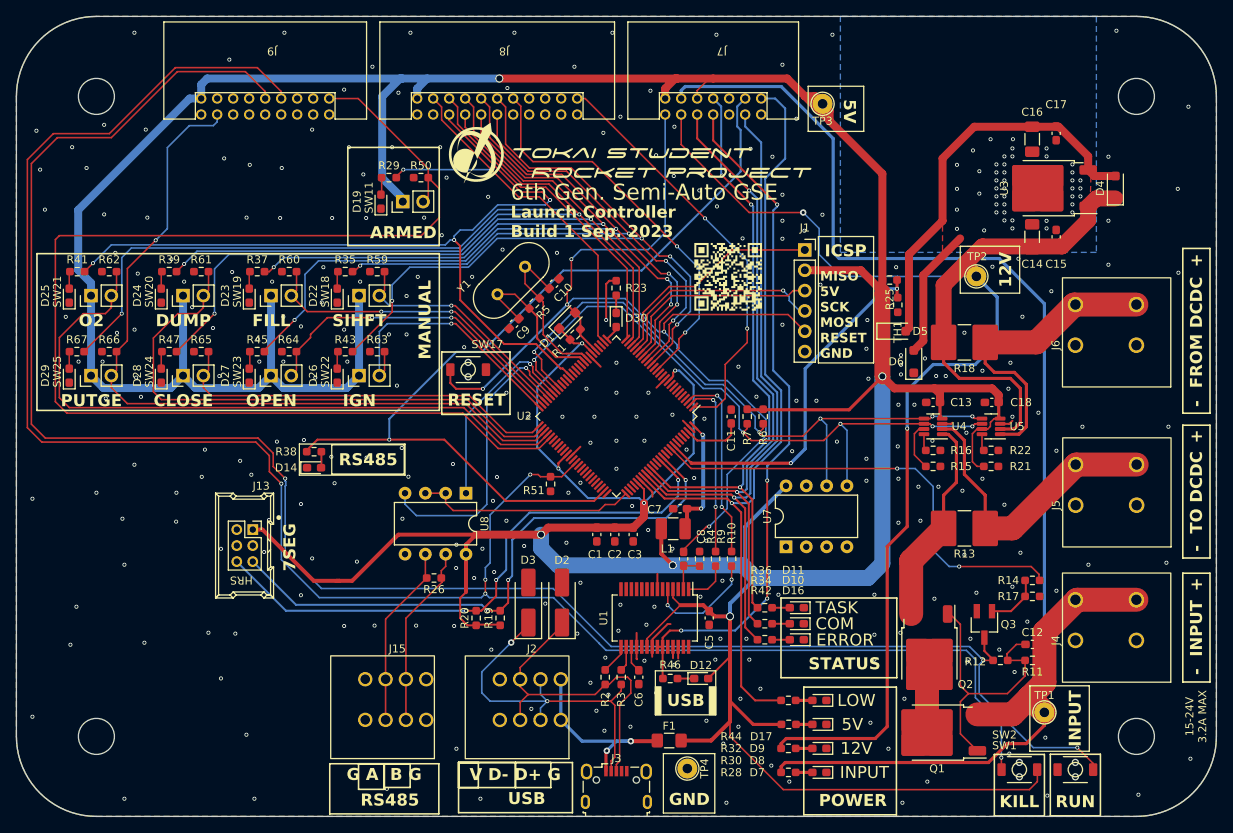
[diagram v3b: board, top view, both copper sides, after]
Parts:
- removed D20, D21: LED_O, LED_SMD:LED_0603_1608Metric_Pad1.05x0.95mm_HandSolder
- removed J14: CONN_BOARD_3, TSRP_Connector_Hirose:DF51A-6DP-2DSA
- removed R31, R33, R52, R54, R55, R56, R57: 1kR, Resistor_SMD:R_0603_1608Metric_Pad0.98x0.95mm_HandSolder
- removed SW12, SW13, SW14, SW15, SW16: SW_Push, Connector_PinHeader_2.54mm:PinHeader_1x02_P2.54mm_Vertical
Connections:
- J8 pad 10: CONN_LED_FB_PURGE -> unconnected-(J8-Pin_10-Pad10)
- J8 pad 19: CONN_LED_SEQUENCE -> unconnected-(J8-Pin_19-Pad19)
- J8 pad 21: CONN_LED_EMERGENCY -> unconnected-(J8-Pin_21-Pad21)
- J8 pad 3: CONN_LED_FB_SHIFT -> unconnected-(J8-Pin_3-Pad3)
- J8 pad 4: CONN_LED_FB_IGNITOR -> unconnected-(J8-Pin_4-Pad4)
- J8 pad 5: CONN_LED_FB_FILL -> unconnected-(J8-Pin_5-Pad5)
- J8 pad 6: CONN_LED_FB_OPEN -> unconnected-(J8-Pin_6-Pad6)
- J8 pad 7: CONN_LED_FB_DUMP -> unconnected-(J8-Pin_7-Pad7)
- J8 pad 8: CONN_LED_FB_CLOSE -> unconnected-(J8-Pin_8-Pad8)
- J8 pad 9: CONN_LED_FB_O2 -> unconnected-(J8-Pin_9-Pad9)
- J9 pad 11: CTL_CLOSE -> unconnected-(J9-Pin_11-Pad11)
- J9 pad 13: CTL_DUMP -> unconnected-(J9-Pin_13-Pad13)
- J9 pad 17: CTL_O2 -> unconnected-(J9-Pin_17-Pad17)
- J9 pad 3: CTL_EMERGENCY_STOP -> unconnected-(J9-Pin_3-Pad3)
- J9 pad 4: CTL_SEQUENCE_START -> unconnected-(J9-Pin_4-Pad4)
- J9 pad 5: CTL_IGNITOR -> unconnected-(J9-Pin_5-Pad5)
- J9 pad 6: CTL_SHIFT -> unconnected-(J9-Pin_6-Pad6)
- J9 pad 7: CTL_OPEN -> unconnected-(J9-Pin_7-Pad7)
- J9 pad 9: CTL_FILL -> unconnected-(J9-Pin_9-Pad9)
- U2 pad 12: Net-(U2-PH0) -> unconnected-(U2-PH0-Pad12)
- U2 pad 13: Net-(U2-PH1) -> unconnected-(U2-PH1-Pad13)
- U2 pad 14: CONN_LED_FB_PURGE -> unconnected-(U2-PH2-Pad14)
- U2 pad 15: CONN_LED_FB_O2 -> unconnected-(U2-PH3-Pad15)
- U2 pad 28: CONN_LED_SEQUENCE -> unconnected-(U2-PG3-Pad28)
- U2 pad 29: CONN_LED_EMERGENCY -> unconnected-(U2-PG4-Pad29)
- U2 pad 4: CONN_LED_FB_IGNITOR -> unconnected-(U2-PE2-Pad4)
- U2 pad 5: CONN_LED_FB_SHIFT -> unconnected-(U2-PE3-Pad5)
- U2 pad 56: CTL_SEQUENCE_START -> unconnected-(U2-PC3-Pad56)
- U2 pad 57: CTL_EMERGENCY_STOP -> unconnected-(U2-PC4-Pad57)
- U2 pad 58: CTL_CONFIRM_3 -> unconnected-(U2-PC5-Pad58)
- U2 pad 59: CTL_CONFIRM_2 -> unconnected-(U2-PC6-Pad59)
- U2 pad 6: CONN_LED_FB_OPEN -> unconnected-(U2-PE4-Pad6)
- U2 pad 60: CTL_CONFIRM_1 -> unconnected-(U2-PC7-Pad60)
- U2 pad 7: CONN_LED_FB_FILL -> unconnected-(U2-PE5-Pad7)
- U2 pad 8: CONN_LED_FB_CLOSE -> unconnected-(U2-PE6-Pad8)
- U2 pad 9: CONN_LED_FB_DUMP -> unconnected-(U2-PE7-Pad9)
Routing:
- net CTL_SEQUENCE_START: track 145.1 -> 0.00 mm
- net CTL_CONFIRM_3: track 139.7 -> 0.00 mm, vias 2 -> 0
- net CTL_EMERGENCY_STOP: track 136.1 -> 0.00 mm
- net CTL_CONFIRM_2: track 130.7 -> 0.00 mm, vias 2 -> 0
- net CTL_CONFIRM_1: track 126.3 -> 0.00 mm, vias 1 -> 0
- net CONN_LED_EMERGENCY: track 71.4 -> 0.00 mm, vias 2 -> 0
- net CTL_IGNITOR: track 95.9 -> 33.5 mm, vias 2 -> 1
- net CONN_LED_SEQUENCE: track 60.5 -> 0.00 mm, vias 2 -> 0
- net CTL_SHIFT: track 82.5 -> 29.6 mm, vias 2 -> 1
- net CONN_LED_FB_IGNITOR: track 52.6 -> 0.00 mm, vias 2 -> 0
- net CONN_LED_FB_OPEN: track 52.2 -> 0.00 mm, vias 2 -> 0
- net CONN_LED_FB_CLOSE: track 50.9 -> 0.00 mm, vias 2 -> 0
- net CONN_LED_FB_PURGE: track 50.1 -> 0.00 mm, vias 2 -> 0
- net (no net): track 0.00 -> 50.1 mm, vias 0 -> 2
- net CONN_LED_FB_SHIFT: track 49.5 -> 0.00 mm, vias 2 -> 0
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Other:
- board text removed: "CONFIRM"
- board text removed: "EMER"
- board text removed: "START"
